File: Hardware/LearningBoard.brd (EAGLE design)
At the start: 90.9 x 91.4 mm, 55 parts, among them IC1 FT230XS-RFT230XS-R

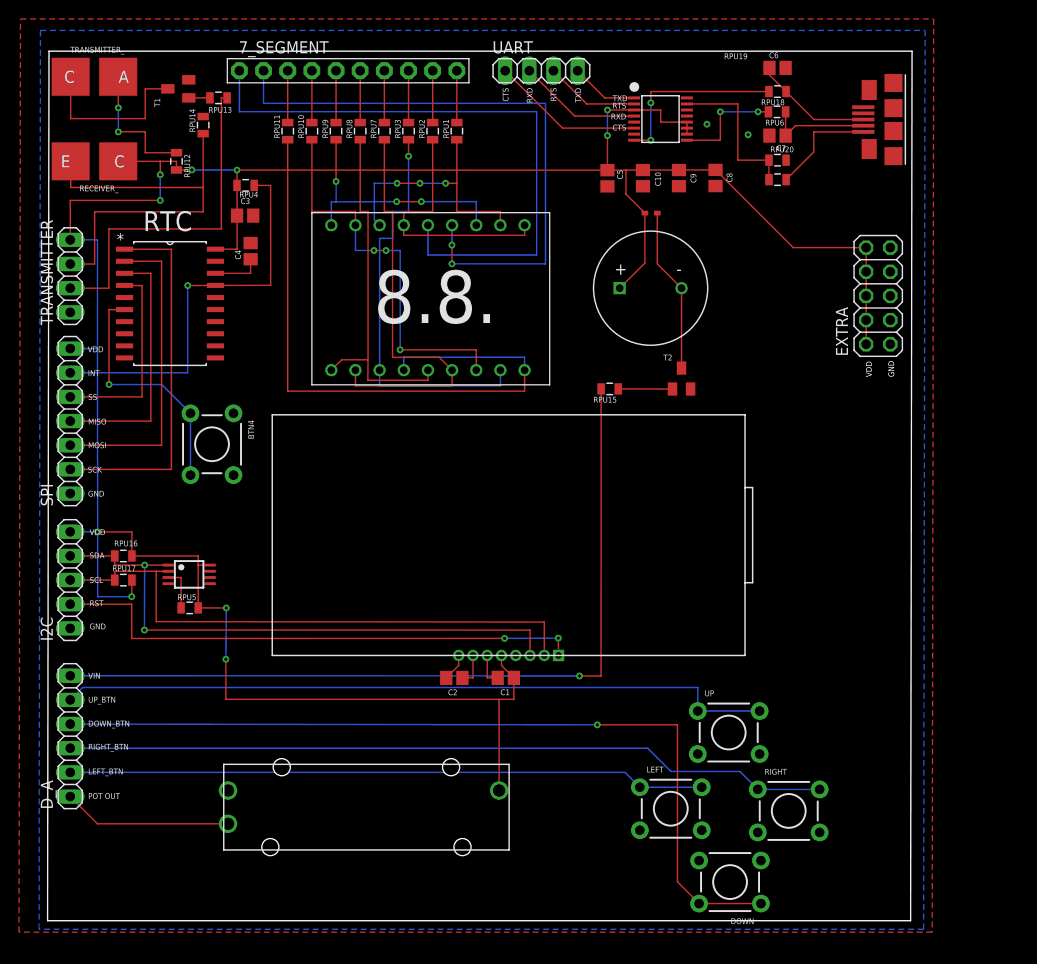
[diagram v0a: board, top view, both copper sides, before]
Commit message: Completed first PCB design ready for OSHPark. REmoved alternate PCB design file created only 1.
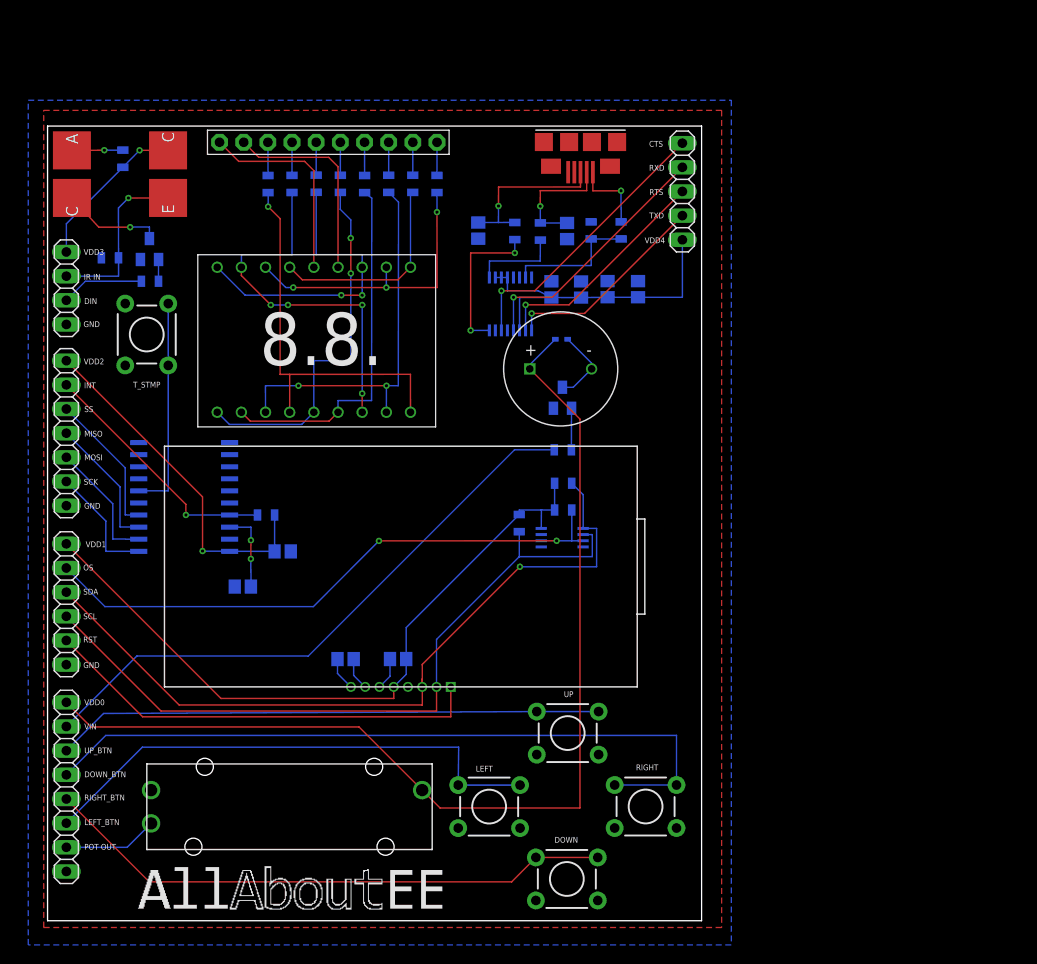
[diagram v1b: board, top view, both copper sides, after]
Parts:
- removed BTN4: (no value), SparkFun-Electromechanical:TACTILE-PTH
- removed EXTRA: (no value), pinhead:2X05
- added T_STMP: (no value), SparkFun-Electromechanical:TACTILE-PTH
- D_A: device pinhead:1X06 -> pinhead:1X08
- I2C: device pinhead:1X05 -> pinhead:1X06
- UART: device pinhead:1X04 -> pinhead:1X05
- moved RPU16 46.9 mm to (54.2, 46.0), flipped to the bottom
- moved RPU17 42.0 mm to (49.6, 41.8), flipped to the bottom, turned to 90 degrees
- moved RPU5 40.6 mm to (54.2, 43.2), flipped to the bottom
- moved U$11 39.4 mm to (54.1, 40.3), flipped to the bottom
- moved C6 35.8 mm to (45.3, 72.6), flipped to the bottom, turned to 270 degrees
- moved C3 35.5 mm to (24.7, 38.8), flipped to the bottom, turned to 180 degrees
- moved C4 35.3 mm to (20.5, 35.1), flipped to the bottom, turned to 0 degrees
- moved RPU4 34.7 mm to (23.0, 42.7), flipped to the bottom
- moved U$10 31.7 mm to (56.0, 80.4), turned to 180 degrees
- moved RPU18 31.3 mm to (49.1, 72.5), flipped to the bottom, turned to 270 degrees
- moved RPU6 27.9 mm to (51.8, 72.5), flipped to the bottom, turned to 270 degrees
- moved IC1 25.0 mm to (48.7, 64.8), flipped to the bottom, turned to 0 degrees
- moved C7 24.3 mm to (54.6, 72.5), flipped to the bottom, turned to 270 degrees
- moved RPU20 20.9 mm to (57.1, 72.6), flipped to the bottom, turned to 90 degrees
- moved RPU13 20.6 mm to (10.8, 67.2), flipped to the bottom
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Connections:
- net N$28 renamed DIN
- removed net N$31: RPU5.2, U$11.3
- new net OS: I2C.5, RPU5.2, U$11.3
- new net VDD_I2C: C1.1, I2C.6, RPU16.2, RPU17.2, RPU5.1, U$11.8, U$2.5
- new net VDD_IR: RECEIVER_.C, RPU12.2, TRANSMITTER.4
- new net VDD_SPI: C3.1, RPU4.1, SPI.7, U$1.20
- new net VDD_UART: C10.1, C5.1, C8.1, C9.1, IC1.10, IC1.11, IC1.12, IC1.3, UART.5
- net LEFT_BTN: now also D_A.3; no longer D_A.2
- net MISO: now also SPI.4, U$1.3; no longer SPI.3, U$1.2
- net MOSI: now also SPI.3, U$1.2; no longer SPI.4, U$1.3
- net N$27: now also T_STMP.3, T_STMP.4; no longer BTN4.3, BTN4.4
- net POT_OUT: now also D_A.2; no longer D_A.1
- net RIGHT_BTN: now also D_A.5; no longer D_A.3
- net UP_BTN: now also D_A.6; no longer D_A.5
- net VDD: now also D_A.8; no longer C1.1, C10.1, C3.1, C5.1, C8.1, C9.1, EXTRA.10, EXTRA.2, EXTRA.4, EXTRA.6, EXTRA.8, I2C.5, IC1.10, IC1.11, IC1.12, IC1.3, RECEIVER_.C, RPU12.2, RPU16.2, RPU17.2, RPU4.1, RPU5.1, SPI.7, TRANSMITTER.4, U$1.20, U$11.8, U$2.5
- net VIN: now also D_A.7; no longer D_A.6
- net VSS: now also D_A.1, T_STMP.1, T_STMP.2; no longer BTN4.1, BTN4.2, EXTRA.1, EXTRA.3, EXTRA.5, EXTRA.7, EXTRA.9
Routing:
- net VDD: track 281.7 -> 111.2 mm, vias 10 -> 0
- net VDD_I2C: track 0.00 -> 74.9 mm
- net OS: track 0.00 -> 62.1 mm, vias 0 -> 2
- net N$23: track 65.2 -> 21.3 mm
- net N$22: track 63.9 -> 21.6 mm, vias 2 -> 0
- net VDD_SPI: track 0.00 -> 37.3 mm, vias 0 -> 1
- net VDD_UART: track 0.00 -> 34.1 mm
- net DOWN_BTN: track 90.1 -> 60.5 mm, vias 1 -> 0
- net DIN: track 36.5 -> 8.71 mm
- net N$13: track 69.0 -> 41.3 mm, vias 0 -> 1
- net SCK: track 38.7 -> 12.5 mm
- net IR_RECEIVER: track 44.3 -> 18.3 mm, vias 0 -> 1
- net VIN: track 86.0 -> 63.3 mm, vias 1 -> 0
- net SDA: track 61.3 -> 80.7 mm, vias 2 -> 1
- net MISO: track 32.8 -> 14.2 mm
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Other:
- board size 90.9 x 91.4 mm -> 68.8 x 83.5 mm
- board text added: "DIN"
- board text added: "IR IN"
- board text added: "OS"
- board text added: "VDD0"
- board text added: "VDD1"
- board text added: "VDD2"
- board text added: "VDD3"
- board text added: "VDD4"
- board text removed: "VDD"

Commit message: - Added some resistor values - Changed resistor names (removed UP string).
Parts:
- R1, R2, R3, R4, R5, R6, R7, R8: value 4.7k -> 62
- R18: value 10k -> 5k
- R9: value 10k -> 768
- renumbered RPU1 to R1, RPU10 to R7, RPU11 to R8, RPU12 to R17, RPU13 to R16, RPU14 to R18, RPU15 to R9, RPU16 to R14, RPU17 to R15, RPU18 to R12, RPU19 to R10, RPU2 to R2, RPU20 to R11, RPU3 to R3, RPU4 to R20, RPU5 to R19, RPU6 to R13, RPU7 to R4, RPU8 to R5, RPU9 to R6, U$5 to POT1

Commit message: New slim design.
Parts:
- removed T2: (no value), transistor:SOT23-BEC
- removed U$8: 254-EMB-140-RO, AllAboutEE:254-EMB-140-RO
- removed U$9: 1N4148X-TP, AllAboutEE:SOD523
- added LED1: (no value), SparkFun-LED:LED5MM
- added VSS: VSS, pinhead:1X01
- D_A: device pinhead:1X08 -> pinhead:1X07
- I2C: device pinhead:1X06 -> pinhead:1X05
- R10: value 4k7 -> 4.7k
- R16: value 10k -> 510
- R17: value 10k -> 30
- R9: value 768 -> 1k
- SPI: device pinhead:1X07 -> pinhead:1X06
- TRANSMITTER: device pinhead:1X04 -> pinhead:1X03
- moved TRANSMITTER_ 116.4 mm to (94.3, 6.81), turned to 90 degrees
- moved R17 104.3 mm to (91.8, 18.2), turned to 90 degrees
- moved T1 101.3 mm to (96.8, 17.3), turned to 180 degrees
- moved RECEIVER_ 97.9 mm to (94.3, 24.5), turned to 270 degrees
- moved R16 97.4 mm to (96.8, 21.4), turned to 180 degrees
- moved R18 96.6 mm to (94.1, 28.8)
- moved T_STMP 84.3 mm to (76.8, 9.59), turned to 270 degrees
- moved TRANSMITTER 81.6 mm to (81.5, 47.8), turned to 180 degrees
- moved I2C 70.3 mm to (70.7, 47.9), turned to 180 degrees
- moved U$10 60.3 mm to (96.4, 35.6), turned to 90 degrees
- moved C6 56.0 mm to (90.4, 39.3), turned to 180 degrees
- moved R10 55.8 mm to (88.7, 24.5), turned to 0 degrees
- moved R11 54.9 mm to (88.7, 27.7), turned to 180 degrees
- moved SPI 54.2 mm to (56.1, 47.9), turned to 180 degrees
- moved R12 53.5 mm to (88.6, 36.4), turned to 0 degrees
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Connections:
- removed net N$29: R9.1, T2.B
- removed net VIN: D_A.7, R9.2
- new net PWM: D_A.6, R9.2
- net CTS: now also UART.4; no longer UART.1
- net DIN: now also TRANSMITTER.1; no longer TRANSMITTER.2
- net DOWN_BTN: now also D_A.2; no longer D_A.4
- net INT: now also SPI.5; no longer SPI.6
- net IR_RECEIVER: now also TRANSMITTER.2; no longer TRANSMITTER.3
- net LEFT_BTN: now also D_A.5; no longer D_A.3
- net MISO: now also SPI.3; no longer SPI.4
- net MOSI: now also SPI.2; no longer SPI.3
- net N$4: now also LED1.A, R9.1; no longer T2.C, U$8.NEGATIVE, U$9.A
- net OS: now also I2C.4; no longer I2C.5
- net POT_OUT: now also D_A.1; no longer D_A.2
- net RIGHT_BTN: now also D_A.3; no longer D_A.5
- net RST: now also I2C.1; no longer I2C.2
- net RTS: now also UART.2; no longer UART.3
- net RXD: now also UART.3; no longer UART.2
- net SCK: now also SPI.1; no longer SPI.2
- net SCL: now also I2C.2; no longer I2C.3
- net SDA: now also I2C.3; no longer I2C.4
- net SS: now also SPI.4; no longer SPI.5
- net TXD: now also UART.1; no longer UART.4
- net UP_BTN: now also D_A.4; no longer D_A.6
- net VDD: now also D_A.7; no longer D_A.8, U$8.POSITIVE, U$9.C
- net VDD_I2C: now also I2C.5; no longer I2C.6
- net VDD_IR: now also TRANSMITTER.3; no longer TRANSMITTER.4
- net VDD_SPI: now also SPI.6; no longer SPI.7
- net VSS: now also LED1.K, VSS.1; no longer D_A.1, I2C.1, SPI.1, T2.E, TRANSMITTER.1
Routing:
- net PWM: track 0.00 -> 79.6 mm, vias 0 -> 2
- net VIN: track 63.3 -> 0.00 mm
- net OS: track 62.1 -> 13.3 mm, vias 2 -> 1
- net VDD: track 111.2 -> 70.1 mm
- net SDA: track 80.7 -> 43.2 mm, vias 1 -> 3
- net N$27: track 22.8 -> 58.7 mm, vias 0 -> 2
- net SCL: track 76.5 -> 41.1 mm
- net POT_OUT: track 9.95 -> 43.0 mm
- net VDD_I2C: track 74.9 -> 42.6 mm
- net DIN: track 8.71 -> 40.0 mm, vias 0 -> 1
- net VDD_IR: track 16.9 -> 43.9 mm, vias 1 -> 3
- net SCK: track 12.5 -> 38.8 mm, vias 0 -> 1
- net RIGHT_BTN: track 77.6 -> 54.3 mm
- net MOSI: track 13.3 -> 35.0 mm, vias 0 -> 1
- net IR_RECEIVER: track 18.3 -> 38.9 mm, vias 1 -> 2
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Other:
- board size 68.8 x 83.5 mm -> 99.5 x 49.9 mm
- board text added: "'A'"
- board text added: "'B'"
- board text added: "'C'"
- board text added: "'D'"
- board text added: "'E'"
- board text added: "'F'"
- board text added: "'G'"
- board text added: "'H'"
- board text added: "D_BTN"
- board text added: "EMBEDDED SYSTEMS LEARNING BOARD"
- board text added: "L DISP."
- board text added: "L_BTN"
- board text added: "PWM"
- board text added: "R DISP."
- board text added: "R_BTN"
- board text added: "Rev. 0C"
- board text added: "U_BTN"
- board text added: "VDD"
- board text added: "VDD_I2C"
- board text added: "VDD_IR"
- board text added: "VDD_SPI"
- board text removed: "DOWN_BTN"
- board text removed: "LEFT_BTN"
- board text removed: "RIGHT_BTN"
- board text removed: "UP_BTN"
- board text removed: "VDD0"
- board text removed: "VDD1"
- board text removed: "VDD2"
- board text removed: "VDD3"
- board text removed: "VDD4"
- board text removed: "VIN"
